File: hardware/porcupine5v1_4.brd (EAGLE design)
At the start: 28.5 x 29.7 mm, 45 parts, among them X1 PROGCON

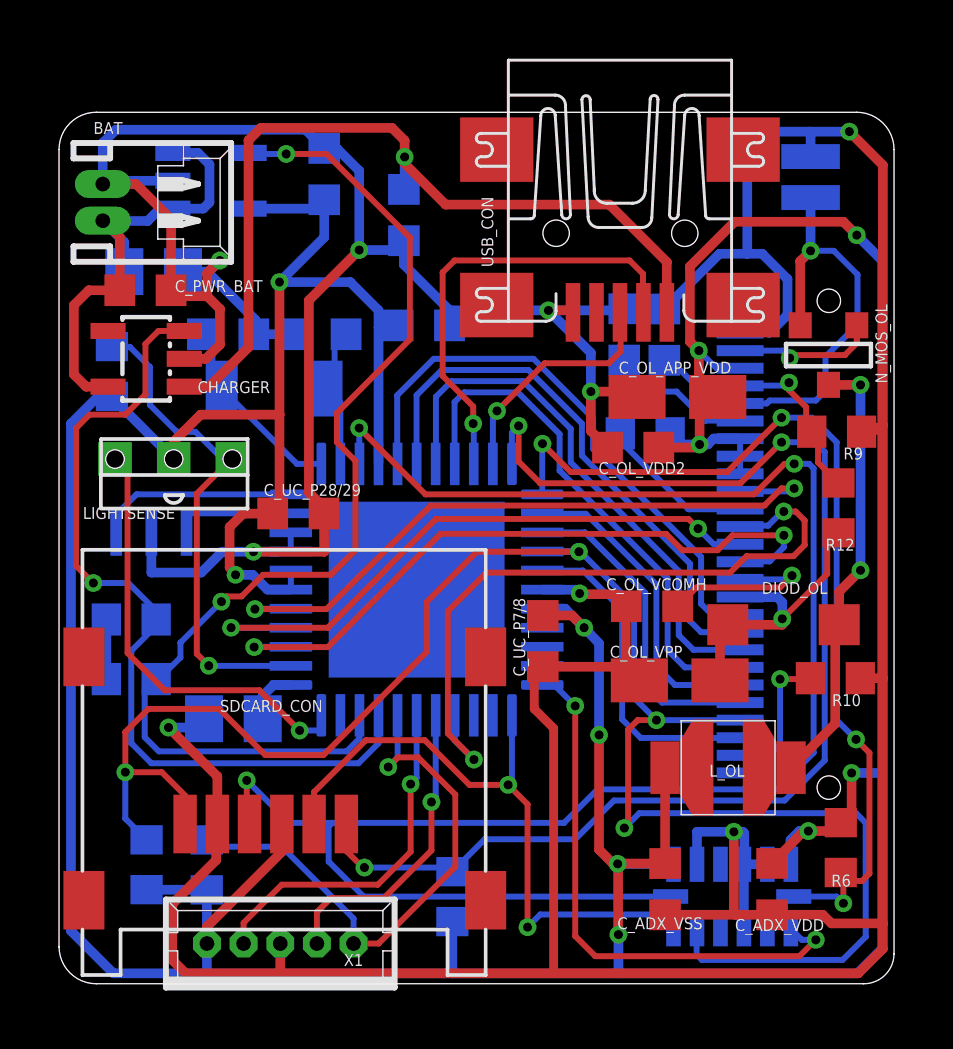
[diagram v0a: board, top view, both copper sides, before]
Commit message: updated hedgehog library and next iteration versions
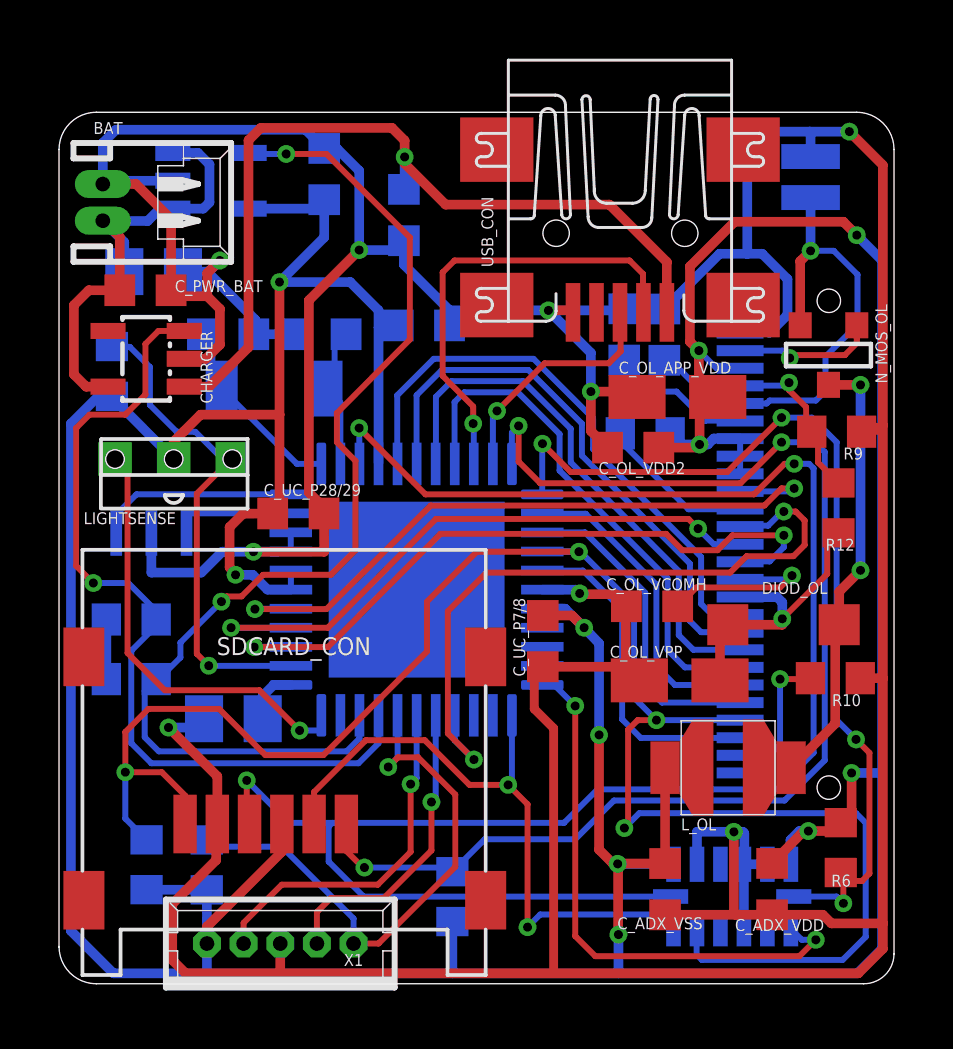
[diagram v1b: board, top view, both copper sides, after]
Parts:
- renumbered U$1 to 12MHZ_RESONATOR
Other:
- board text removed: "SDCARD_CON"
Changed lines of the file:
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@@
 <grid distance="1" unitdist="mil" unit="mil" style="lines" multiple="1" display="yes" altdistance="0.025" altunitdist="inch" altunit="inch"/>
 <layers>
-<layer number="1" name="Top" color="4" fill="1" visible="yes" active="yes"/>
-<layer number="16" name="Bottom" color="1" fill="1" visible="yes" active="yes"/>
-<layer number="17" name="Pads" color="2" fill="1" visible="yes" active="yes"/>
-<layer number="18" name="Vias" color="2" fill="1" visible="yes" active="yes"/>
-<layer number="19" name="Unrouted" color="6" fill="1" visible="yes" active="yes"/>
+<layer number="1" name="Top" color="4" fill="1" visible="no" active="yes"/>
+<layer number="16" name="Bottom" color="1" fill="1" visible="no" active="yes"/>
+<layer number="17" name="Pads" color="2" fill="1" visible="no" active="yes"/>
+<layer number="18" name="Vias" color="2" fill="1" visible="no" active="yes"/>
+<layer number="19" name="Unrouted" color="6" fill="1" visible="no" active="yes"/>
 <layer number="20" name="Dimension" color="15" fill="1" visible="yes" active="yes"/>
 <layer number="21" name="tPlace" color="7" fill="1" visible="yes" active="yes"/>
-<layer number="22" name="bPlace" color="7" fill="1" visible="yes" active="yes"/>
+<layer number="22" name="bPlace" color="7" fill="1" visible="no" active="yes"/>
 <layer number="23" name="tOrigins" color="15" fill="1" visible="yes" active="yes"/>
-<layer number="24" name="bOrigins" color="15" fill="1" visible="yes" active="yes"/>
-<layer number="25" name="tNames" color="7" fill="1" visible="no" active="yes"/>
+<layer number="24" name="bOrigins" color="15" fill="1" visible="no" active="yes"/>
+<layer number="25" name="tNames" color="7" fill="1" visible="yes" active="yes"/>
 <layer number="26" name="bNames" color="7" fill="1" visible="no" active="yes"/>
 <layer number="27" name="tValues" color="7" fill="1" visible="no" active="yes"/>
@@
 <layer number="50" name="dxf" color="7" fill="1" visible="no" active="yes"/>
 <layer number="51" name="tDocu" color="7" fill="1" visible="yes" active="yes"/>
-<layer number="52" name="bDocu" color="7" fill="1" visible="yes" active="yes"/>
+<layer number="52" name="bDocu" color="7" fill="1" visible="no" active="yes"/>
 <layer number="53" name="tGND_GNDA" color="7" fill="9" visible="no" active="no"/>
 <layer number="54" name="bGND_GNDA" color="1" fill="9" visible="no" active="no"/>
@@
 <circle x="41.402" y="25.9334" radius="0.0762" width="0.0254" layer="101"/>
 <rectangle x1="46.5582" y1="7.7978" x2="46.736" y2="7.9756" layer="101"/>
-<text x="0.8128" y="15.8496" size="0.4064" layer="25">LIGHTSENSE</text>
-<text x="5.4864" y="9.271" size="0.4064" layer="25">SDCARD_CON</text>
-<text x="22.1742" y="7.0612" size="0.4064" layer="25">L_OL</text>
+<text x="0.8382" y="15.6718" size="0.4064" layer="25">LIGHTSENSE</text>
+<text x="21.209" y="5.2324" size="0.4064" layer="25">L_OL</text>
 <text x="27.7368" y="15.9004" size="0.4064" layer="26" rot="MR270">OLED</text>
 <text x="9.4742" y="19.0246" size="0.4064" layer="26" rot="MR0">SMD_CRYSTAL</text>
@@
 </autorouter>
 <elements>
-<element name="SDCARD_CON" library="HedgehogLib" package="460DA40013" value="MICROSD_CONN" x="14.5482" y="14.798" rot="R270"/>
+<element name="SDCARD_CON" library="HedgehogLib" package="460DA40013" value="MICROSD_CONN" x="14.5482" y="14.798" smashed="yes" rot="R270">
+<attribute name="VALUE" x="3.1182" y="13.528" size="1.016" layer="27" rot="R270"/>
+<attribute name="NAME" x="10.6324" y="11.817" size="0.6096" layer="25" rot="R180"/>
+</element>
 <element name="LIGHTSENSE" library="HedgehogLib" package="TSL" value="TSL250" x="3.909" y="17.892" smashed="yes"/>
 <element name="USB_CON" library="HedgehogLib" package="248601" value="USBCON" x="19.128" y="25.1442" smashed="yes" rot="R270">
@@
 </element>
 <element name="CHARGER" library="maxim" package="SOT23-5L" value="MAX1551" x="2.9718" y="21.3106" smashed="yes" rot="R90">
-<attribute name="NAME" x="4.7244" y="20.1422" size="0.4064" layer="25"/>
+<attribute name="NAME" x="5.2324" y="19.7866" size="0.4064" layer="25" rot="R90"/>
 <attribute name="VALUE" x="5.6134" y="19.6342" size="0.4064" layer="27" rot="R90"/>
 </element>
@@
 <attribute name="VALUE" x="2.2352" y="18.9738" size="0.4064" layer="28" rot="MR0"/>
 </element>
-<element name="U$1" library="HedgehogLib" package="PRQC-C" value="RESONATORPRQC-C" x="3.1496" y="15.3924" rot="MR180"/>
+<element name="12MHZ_RESONATOR" library="HedgehogLib" package="PRQC-C" value="RESONATORPRQC-C" x="3.1496" y="15.3924" rot="MR180"/>
 </elements>
 <signals>
@@
 <wire x1="23.4696" y1="29.0576" x2="23.4696" y2="24.892" width="0.3302" layer="16"/>
 <contactref element="CON_OLED" pad="P2"/>
-<contactref element="U$1" pad="2_GND"/>
+<contactref element="12MHZ_RESONATOR" pad="2_GND"/>
 <wire x1="24.2206" y1="22.1886" x2="23.2248" y2="22.1886" width="0" layer="19" extent="16-16"/>
 <wire x1="3.1496" y1="14.0208" x2="3.1496" y2="15.3924" width="0.3302" layer="16"/>
@@
 <wire x1="7.9103" y1="16.6894" x2="2.6432" y2="16.6894" width="0.2032" layer="16"/>
 <wire x1="2.6432" y1="16.6894" x2="1.9496" y2="15.9958" width="0.2032" layer="16"/>
-<contactref element="U$1" pad="1"/>
+<contactref element="12MHZ_RESONATOR" pad="1"/>
 <wire x1="1.9496" y1="15.3924" x2="1.9496" y2="15.9958" width="0.2032" layer="16"/>
 </signal>
@@
 <contactref element="PIC_CONTROLLER" pad="32"/>
 <wire x1="7.9023" y1="16.0414" x2="4.3496" y2="16.0414" width="0.2032" layer="16"/>
-<contactref element="U$1" pad="3"/>
+<contactref element="12MHZ_RESONATOR" pad="3"/>
 <wire x1="4.3496" y1="16.0414" x2="4.3496" y2="15.3924" width="0.2032" layer="16"/>
 </signal>
